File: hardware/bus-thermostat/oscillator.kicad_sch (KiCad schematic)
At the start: 15 parts

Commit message: Update some components
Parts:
- added TP3: TestPoint, Connector_Pin:Pin_D0.7mm_L6.5mm_W1.8mm_FlatFork, symbol Connector:TestPoint
- gave numbers to parts that had none: 15
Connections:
- net at C34.2, R42.1, R46.2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: now also TP3.1

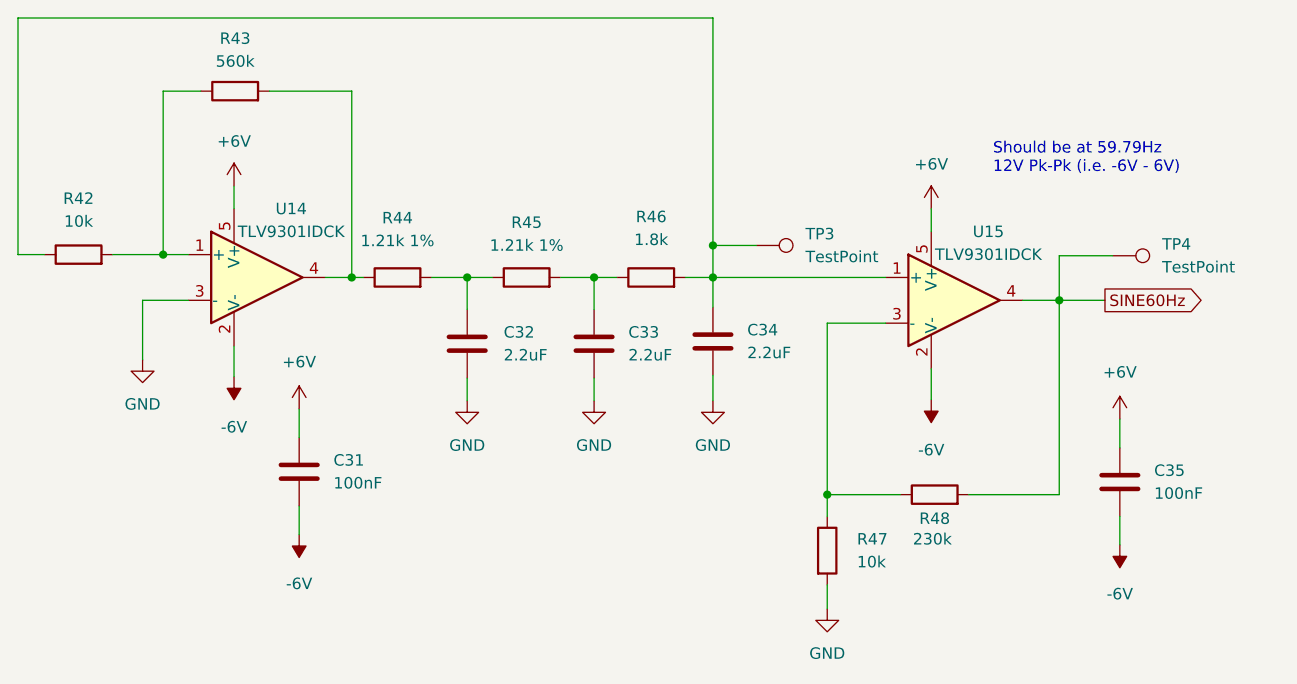
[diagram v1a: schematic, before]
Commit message: Fix oscillator, add fan controller/thermostat and its IOs.
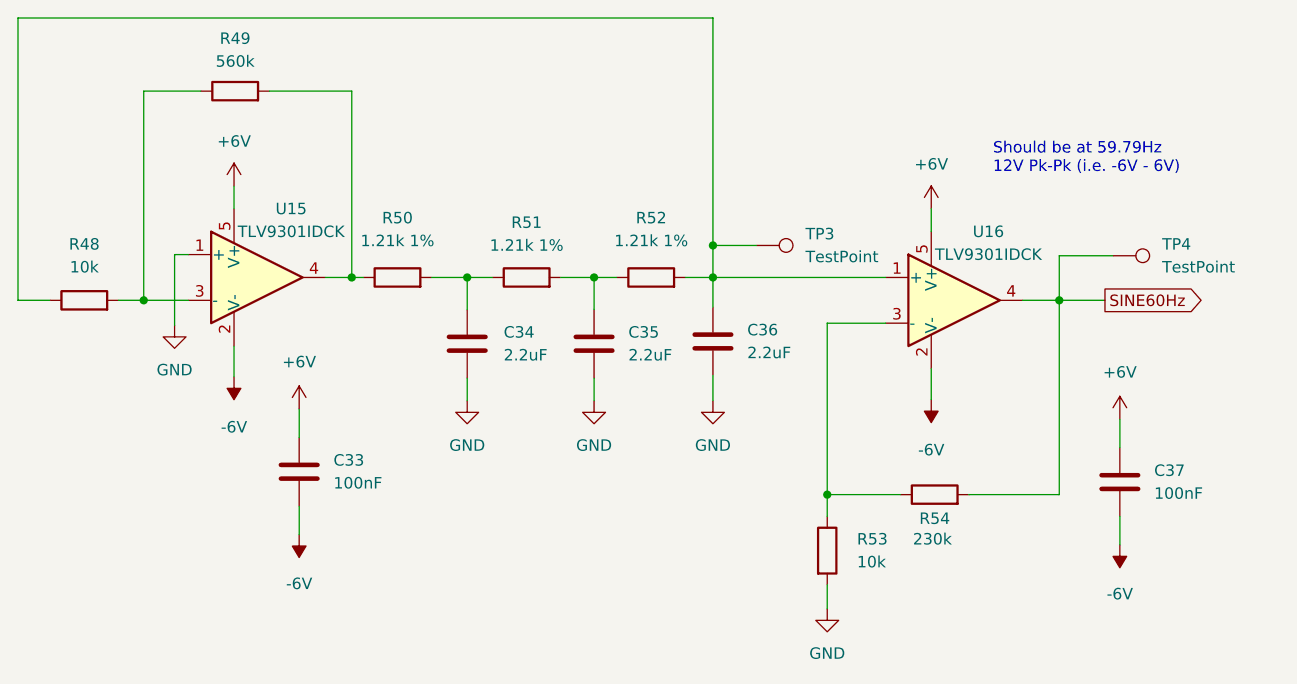
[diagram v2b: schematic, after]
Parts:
- C33: renamed from C31; footprint (none) -> Capacitor_SMD:C_0805_2012Metric_Pad1.18x1.45mm_HandSolder
- C34: renamed from C32; footprint (none) -> Capacitor_SMD:C_0805_2012Metric_Pad1.18x1.45mm_HandSolder
- C35: renamed from C33; footprint (none) -> Capacitor_SMD:C_0805_2012Metric_Pad1.18x1.45mm_HandSolder
- C36: renamed from C34; footprint (none) -> Capacitor_SMD:C_0805_2012Metric_Pad1.18x1.45mm_HandSolder
- C37: renamed from C35; footprint (none) -> Capacitor_SMD:C_0805_2012Metric_Pad1.18x1.45mm_HandSolder
- R48: renamed from R42; footprint (none) -> Resistor_SMD:R_0805_2012Metric_Pad1.20x1.40mm_HandSolder
- R49: renamed from R43; footprint (none) -> Resistor_SMD:R_0805_2012Metric_Pad1.20x1.40mm_HandSolder
- R50: renamed from R44; footprint (none) -> Resistor_SMD:R_0805_2012Metric_Pad1.20x1.40mm_HandSolder
- R51: renamed from R45; footprint (none) -> Resistor_SMD:R_0805_2012Metric_Pad1.20x1.40mm_HandSolder
- R52: renamed from R46; value 1.8k -> 1.21k 1%; footprint (none) -> Resistor_SMD:R_0805_2012Metric_Pad1.20x1.40mm_HandSolder
- R53: renamed from R47; footprint (none) -> Resistor_SMD:R_0805_2012Metric_Pad1.20x1.40mm_HandSolder
- R54: renamed from R48; footprint (none) -> Resistor_SMD:R_0805_2012Metric_Pad1.20x1.40mm_HandSolder
- renumbered U14 to U15, U15 to U16
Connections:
- net GND: now also U15.1 (+); no longer U15.3 (-)
- net at R48.2, R49.1: now also U15.3 (-); no longer U15.1 (+)
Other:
- moved on the sheet: R48
